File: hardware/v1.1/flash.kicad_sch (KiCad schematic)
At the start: 14 parts, among them J6 Micro_SD_Card_Det2, U1 ECP5U_12_CABGA256, U11 W25Q128JVS

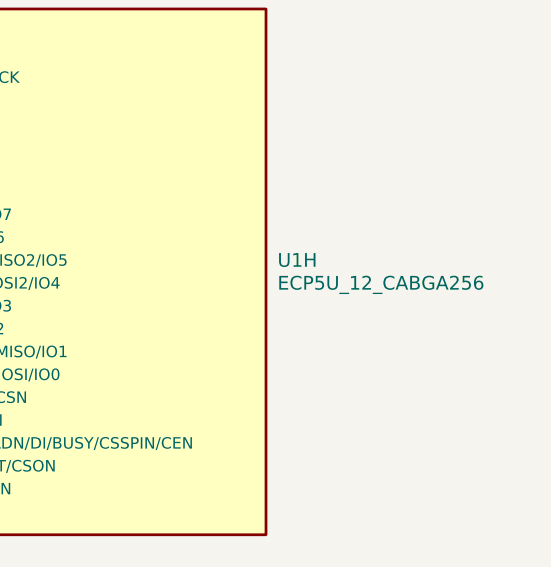
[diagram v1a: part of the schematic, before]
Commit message: Clean up the design by a bit
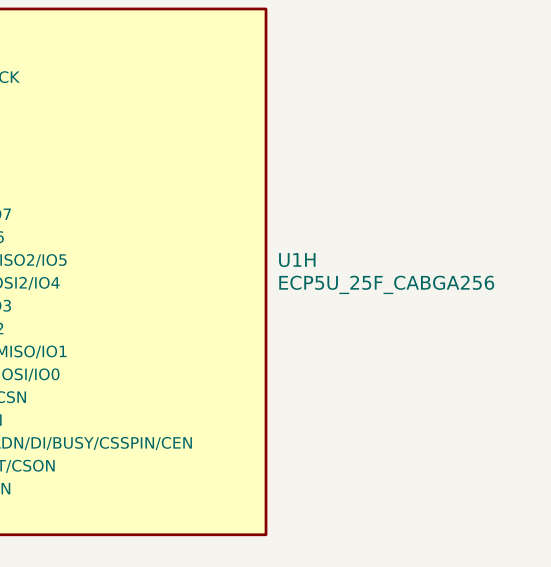
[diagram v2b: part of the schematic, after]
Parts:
- U1: value ECP5U_12_CABGA256 -> ECP5U_25F_CABGA256
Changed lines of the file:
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@@
 			)
 		)
-		(property "Value" "ECP5U_12_CABGA256"
+		(property "Value" "ECP5U_25F_CABGA256"
 			(at 236.22 76.1999 0)
 			(effects
